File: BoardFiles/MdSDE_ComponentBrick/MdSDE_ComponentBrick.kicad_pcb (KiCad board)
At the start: 2 copper layers, 50 parts, among them P101 CONN_01X10, P102 CONN_01X10, SW201 Coded_Switch, SW202 SPST_x3, SW301 Coded_Switch, SW302 SPST_x3, SW401 Coded_Switch, SW402 SPST_x3, SW501 Coded_Switch, SW502 SPST_x3, SW601 Coded_Switch, SW602 SPST_x3, SW701 Coded_Switch, SW702 SPST_x3, SW801 Coded_Switch, SW802 SPST_x3, SW901 Coded_Switch, SW902 SPST_x3

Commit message: updated traces
more updates to the tracks
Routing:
- net GND: track 318.2 -> 297.5 mm
- net Net-(C203-Pad1): track 0.00 -> 14.6 mm, vias 0 -> 2
- net Net-(RV201-Pad1): track 47.3 -> 56.9 mm
- net Pin1: track 77.7 -> 80.2 mm
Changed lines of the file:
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@@
   (general
     (links 115)
-    (no_connects 57)
-    (area 64.470001 54.3 207.038334 105.410001)
+    (no_connects 58)
+    (area 64.444999 54.3 214.658334 114.625002)
     (thickness 1.6)
     (drawings 1)
-    (tracks 354)
+    (tracks 360)
     (zones 0)
     (modules 50)
@@
   (segment (start 84.36 74.39) (end 83.11 75.64) (width 0.25) (layer F.Cu) (net 1))
   (segment (start 83.11 75.64) (end 83.11 77.47) (width 0.25) (layer F.Cu) (net 1))
-  (segment (start 110.49 86.36) (end 110.49 87.63) (width 0.25) (layer F.Cu) (net 2))
-  (segment (start 106.68 91.44) (end 104.14 91.44) (width 0.25) (layer F.Cu) (net 2) (status 800000))
-  (segment (start 110.49 87.63) (end 106.68 91.44) (width 0.25) (layer F.Cu) (net 2))
-  (segment (start 106.68 86.36) (end 110.49 86.36) (width 0.25) (layer F.Cu) (net 2))
-  (segment (start 111.76 81.84) (end 113.59 80.01) (width 0.25) (layer F.Cu) (net 2) (status 800000))
-  (segment (start 111.76 85.09) (end 111.76 81.84) (width 0.25) (layer F.Cu) (net 2))
-  (segment (start 110.49 86.36) (end 111.76 85.09) (width 0.25) (layer F.Cu) (net 2))
+  (segment (start 80.01 83.82) (end 80.01 86.36) (width 0.25) (layer F.Cu) (net 2))
+  (segment (start 80.01 86.36) (end 81.915 88.265) (width 0.25) (layer F.Cu) (net 2))
   (segment (start 106.68 86.36) (end 105.632 86.36) (width 0.25) (layer F.Cu) (net 2))
   (segment (start 105.632 86.36) (end 103.6 88.392) (width 0.25) (layer F.Cu) (net 2) (status 800000))
@@
   (segment (start 73.66 69.85) (end 69.85 69.85) (width 0.25) (layer F.Cu) (net 2))
   (segment (start 80.01 76.2) (end 73.66 69.85) (width 0.25) (layer F.Cu) (net 2))
-  (segment (start 81.915 88.265) (end 81.915 85.725) (width 0.25) (layer F.Cu) (net 2))
   (segment (start 81.28 80.01) (end 83.11 80.01) (width 0.25) (layer F.Cu) (net 2))
   (segment (start 80.01 81.28) (end 81.28 80.01) (width 0.25) (layer F.Cu) (net 2))
   (segment (start 80.01 83.82) (end 80.01 81.28) (width 0.25) (layer F.Cu) (net 2))
-  (segment (start 81.915 85.725) (end 80.01 83.82) (width 0.25) (layer F.Cu) (net 2))
   (segment (start 69.85 92.71) (end 77.47 92.71) (width 0.25) (layer F.Cu) (net 2))
   (segment (start 81.915 88.265) (end 84.36 88.265) (width 0.25) (layer F.Cu) (net 2))
@@
   (via (at 91.44 85.09) (size 0.6) (drill 0.4) (layers F.Cu B.Cu) (net 3))
   (segment (start 90.805 85.725) (end 91.44 85.09) (width 0.25) (layer F.Cu) (net 3))
+  (segment (start 88.36 88.265) (end 92.075 88.265) (width 0.25) (layer F.Cu) (net 4) (status 400000))
+  (segment (start 91.44 80.01) (end 89.61 80.01) (width 0.25) (layer F.Cu) (net 4) (status 800000))
+  (segment (start 92.71 81.28) (end 91.44 80.01) (width 0.25) (layer F.Cu) (net 4))
+  (via (at 92.71 81.28) (size 0.6) (drill 0.4) (layers F.Cu B.Cu) (net 4))
+  (segment (start 92.71 87.63) (end 92.71 81.28) (width 0.25) (layer B.Cu) (net 4))
+  (via (at 92.71 87.63) (size 0.6) (drill 0.4) (layers F.Cu B.Cu) (net 4))
+  (segment (start 92.075 88.265) (end 92.71 87.63) (width 0.25) (layer F.Cu) (net 4))
   (segment (start 99.6 74.295) (end 99.6 74.39) (width 0.25) (layer F.Cu) (net 5))
   (segment (start 99.6 74.39) (end 98.35 75.64) (width 0.25) (layer F.Cu) (net 5))
@@
   (segment (start 191.04 74.39) (end 189.79 75.64) (width 0.25) (layer F.Cu) (net 23))
   (segment (start 189.79 75.64) (end 189.79 77.47) (width 0.25) (layer F.Cu) (net 23))
-  (segment (start 89.61 82.55) (end 92.71 82.55) (width 0.25) (layer F.Cu) (net 26))
-  (segment (start 92.71 82.55) (end 92.71 87.63) (width 0.25) (layer B.Cu) (net 26))
-  (via (at 92.71 82.55) (size 0.6) (drill 0.4) (layers F.Cu B.Cu) (net 26))
+  (segment (start 89.61 82.55) (end 93.98 82.55) (width 0.25) (layer F.Cu) (net 26) (status 400000))
+  (segment (start 92.71 102.87) (end 91.44 102.87) (width 0.25) (layer B.Cu) (net 26))
+  (segment (start 93.98 101.6) (end 92.71 102.87) (width 0.25) (layer B.Cu) (net 26))
+  (segment (start 93.98 82.55) (end 93.98 101.6) (width 0.25) (layer B.Cu) (net 26))
+  (via (at 93.98 82.55) (size 0.6) (drill 0.4) (layers F.Cu B.Cu) (net 26))
   (segment (start 69.85 72.39) (end 73.66 72.39) (width 0.25) (layer B.Cu) (net 26))
   (segment (start 73.66 72.39) (end 78.74 77.47) (width 0.25) (layer B.Cu) (net 26))
@@
   (segment (start 78.74 101.6) (end 80.01 102.87) (width 0.25) (layer B.Cu) (net 26))
   (segment (start 80.01 102.87) (end 91.44 102.87) (width 0.25) (layer B.Cu) (net 26))
-  (segment (start 91.44 102.87) (end 92.71 101.6) (width 0.25) (layer B.Cu) (net 26))
-  (segment (start 92.71 101.6) (end 92.71 87.63) (width 0.25) (layer B.Cu) (net 26))
   (segment (start 80.01 102.87) (end 83.82 99.06) (width 0.25) (layer B.Cu) (net 26))
   (segment (start 69.85 74.93) (end 73.66 74.93) (width 0.25) (layer B.Cu) (net 27))
@@
   (segment (start 212.09 91.44) (end 212.09 97.79) (width 0.25) (layer F.Cu) (net 41))
   (segment (start 210.82 90.17) (end 212.09 91.44) (width 0.25) (layer F.Cu) (net 41))
-  (segment (start 85.36 66.58) (end 85.36 64.5) (width 0.25) (layer F.Cu) (net 42))
-  (segment (start 93.98 93.98) (end 88.9 99.06) (width 0.25) (layer F.Cu) (net 42))
-  (segment (start 93.98 66.04) (end 93.98 93.98) (width 0.25) (layer F.Cu) (net 42))
-  (segment (start 91.44 63.5) (end 93.98 66.04) (width 0.25) (layer F.Cu) (net 42))
+  (segment (start 85.36 66.58) (end 85.36 64.5) (width 0.25) (layer F.Cu) (net 42) (status 400000))
+  (segment (start 85.36 64.5) (end 86.36 63.5) (width 0.25) (layer F.Cu) (net 42))
+  (segment (start 86.36 63.5) (end 91.44 63.5) (width 0.25) (layer F.Cu) (net 42))
+  (segment (start 91.44 63.5) (end 96.52 68.58) (width 0.25) (layer F.Cu) (net 42))
+  (segment (start 96.52 68.58) (end 96.52 76.2) (width 0.25) (layer F.Cu) (net 42))
+  (segment (start 96.52 76.2) (end 93.98 78.74) (width 0.25) (layer F.Cu) (net 42))
+  (segment (start 93.98 78.74) (end 93.98 80.01) (width 0.25) (layer F.Cu) (net 42))
+  (segment (start 93.98 80.01) (end 95.25 81.28) (width 0.25) (layer F.Cu) (net 42))
+  (segment (start 95.25 81.28) (end 95.25 92.71) (width 0.25) (layer F.Cu) (net 42))
+  (segment (start 95.25 92.71) (end 88.9 99.06) (width 0.25) (layer F.Cu) (net 42) (status 800000))
   (segment (start 86.36 63.5) (end 91.44 63.5) (width 0.25) (layer F.Cu) (net 42))
   (segment (start 85.36 64.5) (end 86.36 63.5) (width 0.25) (layer F.Cu) (net 42))

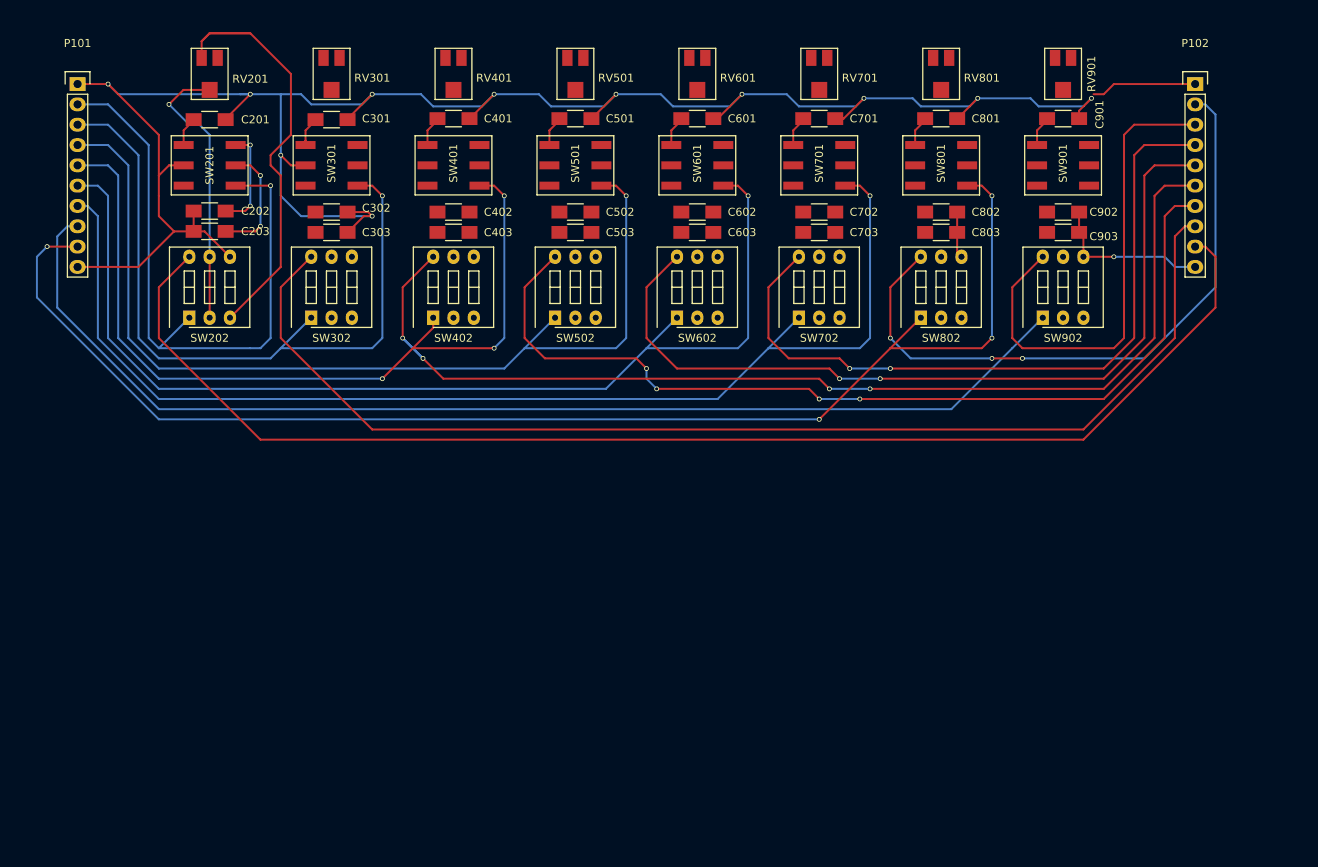
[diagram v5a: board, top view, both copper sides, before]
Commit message: Finished PCB Layout for component brick
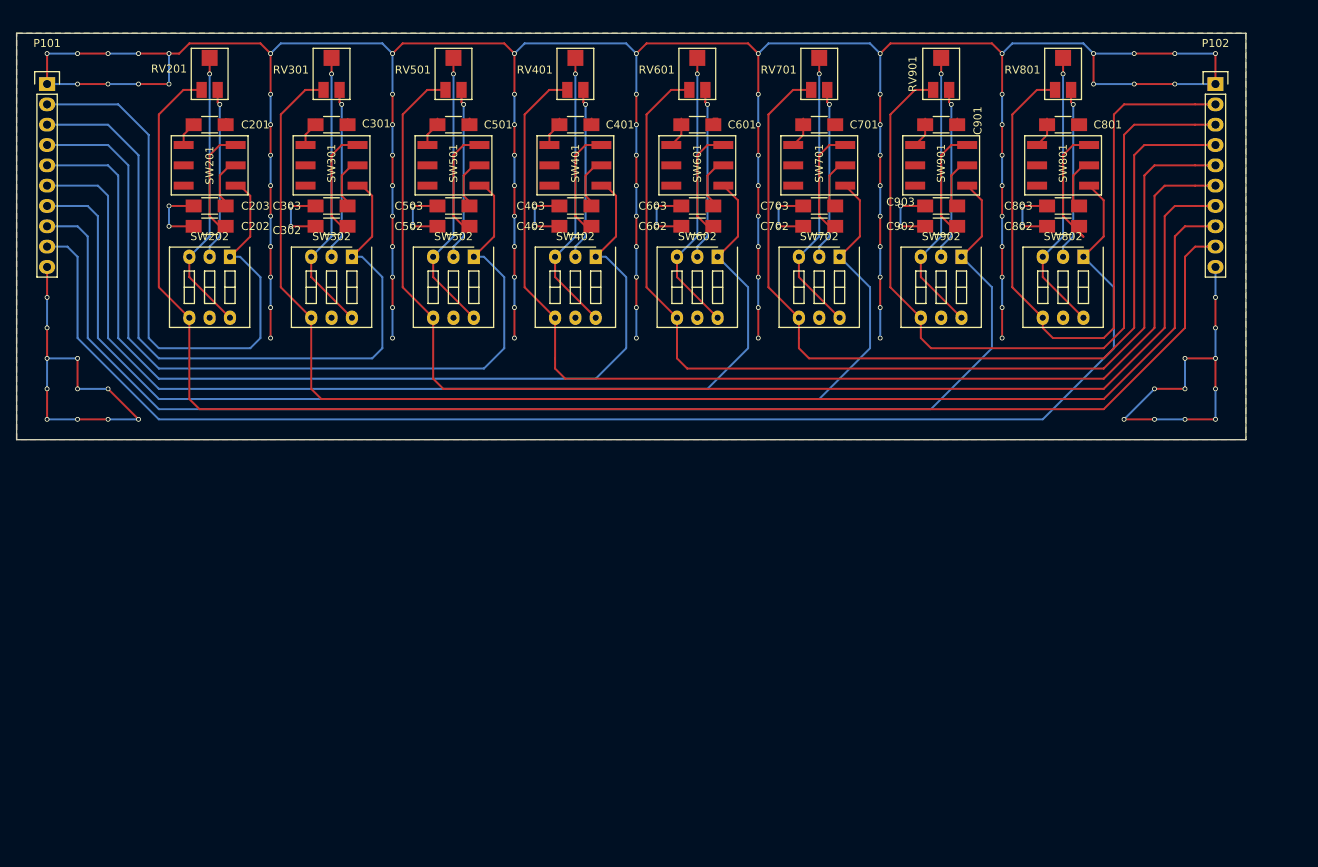
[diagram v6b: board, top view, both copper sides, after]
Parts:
- SW202, SW302, SW402, SW502, SW602, SW702, SW802, SW902: footprint Buttons_Switches_ThroughHole:SW_DIP_x3_Slide -> Footprints:SW_DIP_x3_Slide
- moved SW802 21.7 mm to (195.6, 91.4), turned to 180 degrees
- moved SW402 21.7 mm to (134.6, 91.4), turned to 180 degrees
- moved C403 15.6 mm to (132.1, 85.1), turned to 180 degrees
- moved C503 15.6 mm to (116.8, 85.1), turned to 180 degrees
- moved C803 15.6 mm to (193.0, 85.1), turned to 180 degrees
- moved C903 15.6 mm to (177.8, 85.1), turned to 180 degrees
- moved C402 15.3 mm to (132.1, 87.6), turned to 180 degrees
- moved C502 15.3 mm to (116.8, 87.6), turned to 180 degrees
- moved C802 15.3 mm to (193.0, 87.6), turned to 180 degrees
- moved C902 15.3 mm to (177.8, 87.6), turned to 180 degrees
- moved C401 15.3 mm to (132.1, 74.9)
- moved C501 15.3 mm to (116.8, 74.9)
- moved C801 15.3 mm to (193.0, 74.9)
- moved C901 15.3 mm to (177.8, 74.9)
- moved RV401 15.2 mm to (132.1, 68.6), turned to 180 degrees
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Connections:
- RV201 pad 3: (no net) -> Src1
- RV301 pad 3: (no net) -> Src2
- RV401 pad 3: (no net) -> Src4
- RV501 pad 3: (no net) -> Src3
- RV601 pad 3: (no net) -> Src5
- RV701 pad 3: (no net) -> Src6
- RV801 pad 3: (no net) -> Src8
- RV901 pad 3: (no net) -> Src7
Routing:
- net GND: track 297.5 -> 614.5 mm, vias 12 -> 124
- net Src3: track 118.4 -> 157.2 mm, vias 4 -> 0
- net Src7: track 61.6 -> 99.2 mm
- net Net-(RV901-Pad2): track 0.00 -> 35.6 mm, vias 0 -> 1
- net Net-(RV401-Pad2): track 0.00 -> 35.6 mm, vias 0 -> 1
- net Net-(RV801-Pad2): track 0.00 -> 35.6 mm, vias 0 -> 1
- net Net-(RV601-Pad2): track 0.00 -> 35.6 mm, vias 0 -> 1
- net Net-(RV501-Pad2): track 0.00 -> 35.6 mm, vias 0 -> 1
- net Net-(RV301-Pad2): track 0.00 -> 35.6 mm, vias 0 -> 1
- net Net-(RV701-Pad2): track 0.00 -> 35.6 mm, vias 0 -> 1
- net Net-(RV201-Pad1): track 56.9 -> 21.5 mm, vias 0 -> 1
- net Src2: track 148.7 -> 171.7 mm
- net Src5: track 105.4 -> 128.2 mm, vias 2 -> 0
- net Src6: track 91.6 -> 113.7 mm, vias 2 -> 0
- net Net-(RV801-Pad1): track 0.00 -> 21.5 mm, vias 0 -> 1
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- added copper zone on B.Cu, net GND
- added copper zone on F.Cu, net GND
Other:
- board outline added: 153.7 x 50.8 mm

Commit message: Built motor driver carrier
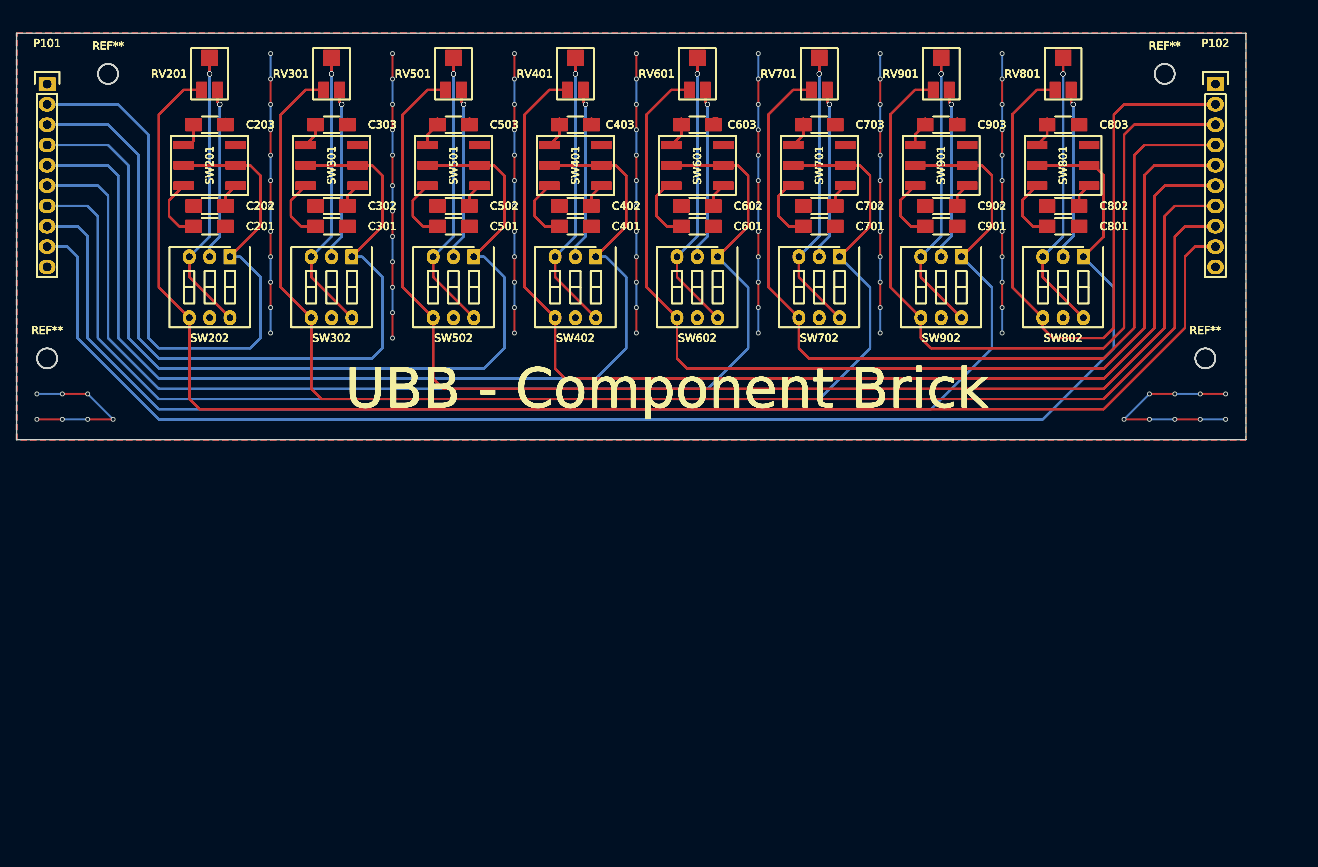
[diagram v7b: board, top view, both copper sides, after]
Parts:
- added C201 (x3): C_Small, Capacitors_SMD:C_1206_HandSoldering, F.Cu at (86.4, 87.6)
- added C202 (x3): C_Small, Capacitors_SMD:C_1206_HandSoldering, F.Cu at (86.4, 85.1)
- added C203 (x3): C_Small, Capacitors_SMD:C_1206_HandSoldering, F.Cu at (86.4, 74.9)
- added C301 (x3): C_Small, Capacitors_SMD:C_1206_HandSoldering, F.Cu at (101.6, 87.6)
- added C302 (x3): C_Small, Capacitors_SMD:C_1206_HandSoldering, F.Cu at (101.6, 85.1)
- added C303 (x3): C_Small, Capacitors_SMD:C_1206_HandSoldering, F.Cu at (101.6, 74.9)
- added C401 (x3): C_Small, Capacitors_SMD:C_1206_HandSoldering, F.Cu at (132.1, 87.6)
- added C402 (x3): C_Small, Capacitors_SMD:C_1206_HandSoldering, F.Cu at (132.1, 85.1)
- added C403 (x3): C_Small, Capacitors_SMD:C_1206_HandSoldering, F.Cu at (132.1, 74.9)
- added C501 (x3): C_Small, Capacitors_SMD:C_1206_HandSoldering, F.Cu at (116.8, 87.6)
- added C502 (x3): C_Small, Capacitors_SMD:C_1206_HandSoldering, F.Cu at (116.8, 85.1)
- added C503 (x3): C_Small, Capacitors_SMD:C_1206_HandSoldering, F.Cu at (116.8, 74.9)
- added C601 (x3): C_Small, Capacitors_SMD:C_1206_HandSoldering, F.Cu at (147.3, 87.6)
- added C602 (x3): C_Small, Capacitors_SMD:C_1206_HandSoldering, F.Cu at (147.3, 85.1)
- added C603 (x3): C_Small, Capacitors_SMD:C_1206_HandSoldering, F.Cu at (147.3, 74.9)
- added C701 (x3): C_Small, Capacitors_SMD:C_1206_HandSoldering, F.Cu at (162.6, 87.6)
- added C702 (x3): C_Small, Capacitors_SMD:C_1206_HandSoldering, F.Cu at (162.6, 85.1)
- added C703 (x3): C_Small, Capacitors_SMD:C_1206_HandSoldering, F.Cu at (162.6, 74.9)
- added C801 (x3): C_Small, Capacitors_SMD:C_1206_HandSoldering, F.Cu at (193.0, 87.6)
- added C802 (x3): C_Small, Capacitors_SMD:C_1206_HandSoldering, F.Cu at (193.0, 85.1)
- added C803 (x3): C_Small, Capacitors_SMD:C_1206_HandSoldering, F.Cu at (193.0, 74.9)
- added C901 (x3): C_Small, Capacitors_SMD:C_1206_HandSoldering, F.Cu at (177.8, 87.6)
- added C902 (x3): C_Small, Capacitors_SMD:C_1206_HandSoldering, F.Cu at (177.8, 85.1)
- added C903 (x3): C_Small, Capacitors_SMD:C_1206_HandSoldering, F.Cu at (177.8, 74.9)
- added P101 (x3): CONN_01X10, Pin_Headers:Pin_Header_Straight_1x10, F.Cu at (66.0, 69.8)
- added P102 (x3): CONN_01X10, Pin_Headers:Pin_Header_Straight_1x10, F.Cu at (212.1, 69.8)
- added REF** (x4): MountingHole_2.5mm, Mounting_Holes:MountingHole_2.5mm, F.Cu at (66.0, 104.1)
- added REF** (x4): MountingHole_2.5mm, Mounting_Holes:MountingHole_2.5mm, F.Cu at (210.8, 104.1)
- added REF** (x4): MountingHole_2.5mm, Mounting_Holes:MountingHole_2.5mm, F.Cu at (205.7, 68.6)
- added REF** (x4): MountingHole_2.5mm, Mounting_Holes:MountingHole_2.5mm, F.Cu at (73.7, 68.6)
- added RV201 (x3): POT, Footprints:3314_Potentiometer, F.Cu at (86.4, 68.6)
- added RV301 (x3): POT, Footprints:3314_Potentiometer, F.Cu at (101.6, 68.6)
- added RV401 (x3): POT, Footprints:3314_Potentiometer, F.Cu at (132.1, 68.6)
- added RV501 (x3): POT, Footprints:3314_Potentiometer, F.Cu at (116.8, 68.6)
- added RV601 (x3): POT, Footprints:3314_Potentiometer, F.Cu at (147.3, 68.6)
- added RV701 (x3): POT, Footprints:3314_Potentiometer, F.Cu at (162.6, 68.6)
- added RV801 (x3): POT, Footprints:3314_Potentiometer, F.Cu at (193.0, 68.6)
- added RV901 (x3): POT, Footprints:3314_Potentiometer, F.Cu at (177.8, 68.6)
- added SW201 (x3): Coded_Switch, Footprints:SH-7000RotarySwitch, F.Cu at (86.4, 80.0)
- added SW202 (x3): SPST_x3, Footprints:SW_DIP_x3_Slide, F.Cu at (88.9, 91.4)
- added SW301 (x3): Coded_Switch, Footprints:SH-7000RotarySwitch, F.Cu at (101.6, 80.0)
- added SW302 (x3): SPST_x3, Footprints:SW_DIP_x3_Slide, F.Cu at (104.1, 91.4)
- added SW401 (x3): Coded_Switch, Footprints:SH-7000RotarySwitch, F.Cu at (132.1, 80.0)
- added SW402 (x3): SPST_x3, Footprints:SW_DIP_x3_Slide, F.Cu at (134.6, 91.4)
- added SW501 (x3): Coded_Switch, Footprints:SH-7000RotarySwitch, F.Cu at (116.8, 80.0)
- added SW502 (x3): SPST_x3, Footprints:SW_DIP_x3_Slide, F.Cu at (119.4, 91.4)
- added SW601 (x3): Coded_Switch, Footprints:SH-7000RotarySwitch, F.Cu at (147.3, 80.0)
- added SW602 (x3): SPST_x3, Footprints:SW_DIP_x3_Slide, F.Cu at (149.9, 91.4)
- added SW701 (x3): Coded_Switch, Footprints:SH-7000RotarySwitch, F.Cu at (162.6, 80.0)
- added SW702 (x3): SPST_x3, Footprints:SW_DIP_x3_Slide, F.Cu at (165.1, 91.4)
- added SW801 (x3): Coded_Switch, Footprints:SH-7000RotarySwitch, F.Cu at (193.0, 80.0)
- added SW802 (x3): SPST_x3, Footprints:SW_DIP_x3_Slide, F.Cu at (195.6, 91.4)
- added SW901 (x3): Coded_Switch, Footprints:SH-7000RotarySwitch, F.Cu at (177.8, 80.0)
- added SW902 (x3): SPST_x3, Footprints:SW_DIP_x3_Slide, F.Cu at (180.3, 91.4)
- moved C201 12.7 mm to (86.4, 87.6)
- moved C301 12.7 mm to (101.6, 87.6)
- moved C401 12.7 mm to (132.1, 87.6)
- moved C501 12.7 mm to (116.8, 87.6)
- moved C601 12.7 mm to (147.3, 87.6)
- moved C701 12.7 mm to (162.6, 87.6)
- moved C801 12.7 mm to (193.0, 87.6)
- moved C901 12.7 mm to (177.8, 87.6)
- moved C203 10.2 mm to (86.4, 74.9), turned to 0 degrees
- moved C303 10.2 mm to (101.6, 74.9), turned to 0 degrees
- moved C403 10.2 mm to (132.1, 74.9), turned to 0 degrees
- moved C503 10.2 mm to (116.8, 74.9), turned to 0 degrees
- moved C603 10.2 mm to (147.3, 74.9), turned to 0 degrees
- moved C703 10.2 mm to (162.6, 74.9), turned to 0 degrees
- moved C803 10.2 mm to (193.0, 74.9), turned to 0 degrees
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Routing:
- net Pin8: track 176.4 -> 745.9 mm
- net Src1: track 186.2 -> 744.7 mm
- net Pin7: track 162.6 -> 698.1 mm
- net Src2: track 171.7 -> 686.8 mm
- net Pin6: track 148.1 -> 640.0 mm
- net Src3: track 157.2 -> 628.8 mm
- net Pin5: track 134.4 -> 585.0 mm
- net Src4: track 143.3 -> 573.2 mm
- net Pin4: track 121.7 -> 533.0 mm
- net Src5: track 128.2 -> 512.8 mm
- net Pin3: track 107.2 -> 475.0 mm
- net Src6: track 113.7 -> 454.8 mm
- net Pin2: track 92.7 -> 417.0 mm
- net Src7: track 99.2 -> 396.8 mm
- net GND: track 614.5 -> 322.7 mm, vias 124 -> 100
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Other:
- board text added: "SMU Senior Design: Universal Biasing Board Team Members: Logan Campbell, Josh Dimayuga, Jeff Limbocker, Gerardo Padierna"
- board text added: "UBB - Component Brick"
